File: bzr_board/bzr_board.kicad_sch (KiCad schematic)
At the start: 13 parts, among them J1 Conn_01x06, U1 74HC00

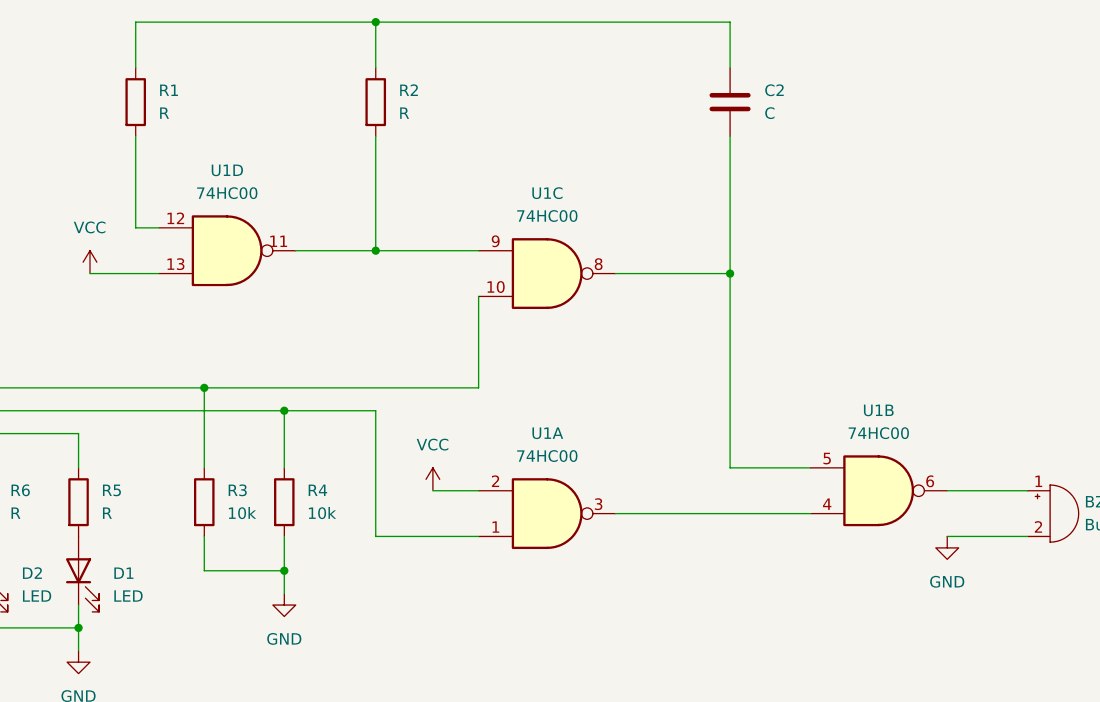
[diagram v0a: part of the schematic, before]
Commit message: bzr_board: update schematics and assign footprints
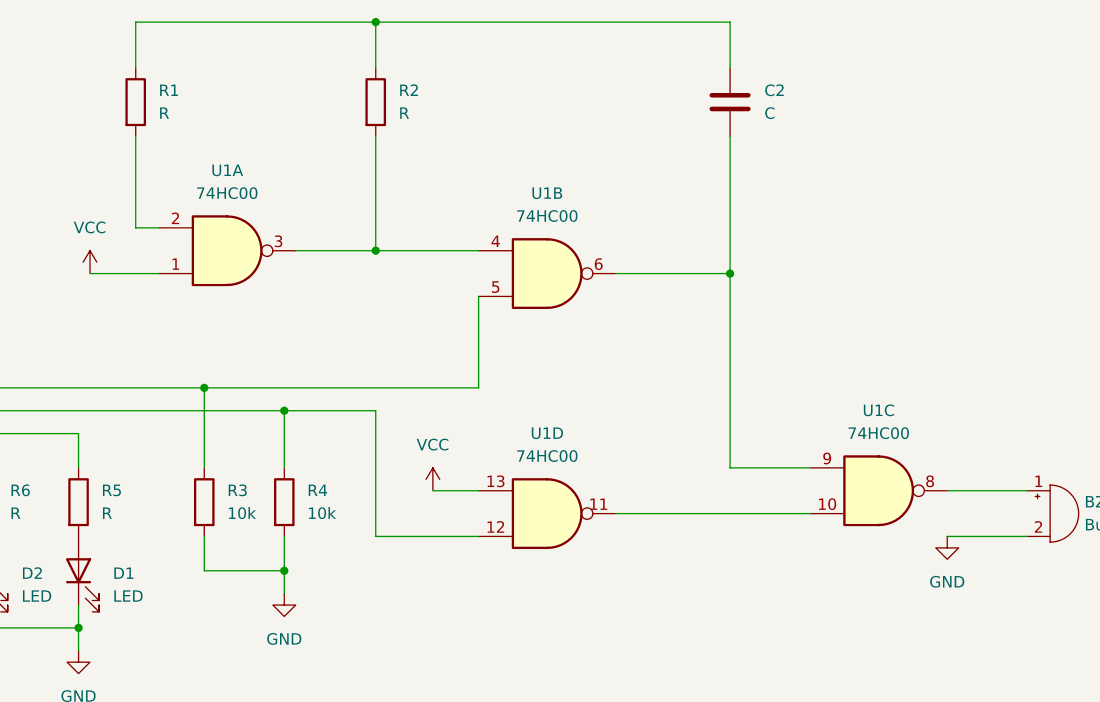
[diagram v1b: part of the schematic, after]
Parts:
- BZ1: footprint (none) -> Buzzer_Beeper:Buzzer_TDK_PS1240P02BT_D12.2mm_H6.5mm
- C1, C2: footprint (none) -> Capacitor_SMD:C_0805_2012Metric_Pad1.18x1.45mm_HandSolder
- D1, D2: footprint (none) -> LED_SMD:LED_0805_2012Metric_Pad1.15x1.40mm_HandSolder
- J1: footprint (none) -> Connector_PinHeader_2.54mm:PinHeader_1x06_P2.54mm_Vertical
- R1: footprint (none) -> Resistor_SMD:R_0603_1608Metric_Pad0.98x0.95mm_HandSolder
- R2, R3, R4, R5, R6: footprint (none) -> Resistor_SMD:R_0805_2012Metric_Pad1.20x1.40mm_HandSolder
- U1: footprint (none) -> Package_SO:SO-14_5.3x10.2mm_P1.27mm
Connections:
- net VCC: now also U1.1; no longer U1.2
- net auto: now also U1.5; no longer U1.10
- net manual: now also U1.12; no longer U1.1
- net at BZ1.1 (-): now also U1.8; no longer U1.6
- net at R1.2: now also U1.2; no longer U1.12
- net at U1.3, U1.4: now also R2.2
- new net: U1.10, U1.11
- new net: C2.2, U1.6, U1.9
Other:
- moved on the sheet: U1A, U1B, U1C, U1D

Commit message: bzr_board: add board design
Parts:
- R1: footprint Resistor_SMD:R_0603_1608Metric_Pad0.98x0.95mm_HandSolder -> Resistor_SMD:R_0805_2012Metric_Pad1.20x1.40mm_HandSolder
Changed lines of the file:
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@@
       (effects (font (size 1.27 1.27)) (justify left))
     )
-    (property "Footprint" "Resistor_SMD:R_0603_1608Metric_Pad0.98x0.95mm_HandSolder" (id 2) (at 109.982 38.1 90)
+    (property "Footprint" "Resistor_SMD:R_0805_2012Metric_Pad1.20x1.40mm_HandSolder" (id 2) (at 109.982 38.1 90)
       (effects (font (size 1.27 1.27)) hide)
     )
@@
     )
     (path "/fe3afa16-4331-4114-bcf8-f31acd774c30"
-      (reference "R1") (unit 1) (value "R") (footprint "Resistor_SMD:R_0603_1608Metric_Pad0.98x0.95mm_HandSolder")
+      (reference "R1") (unit 1) (value "R") (footprint "Resistor_SMD:R_0805_2012Metric_Pad1.20x1.40mm_HandSolder")
     )
     (path "/cccd4cea-c88e-4fc0-907f-447edef8bc42"

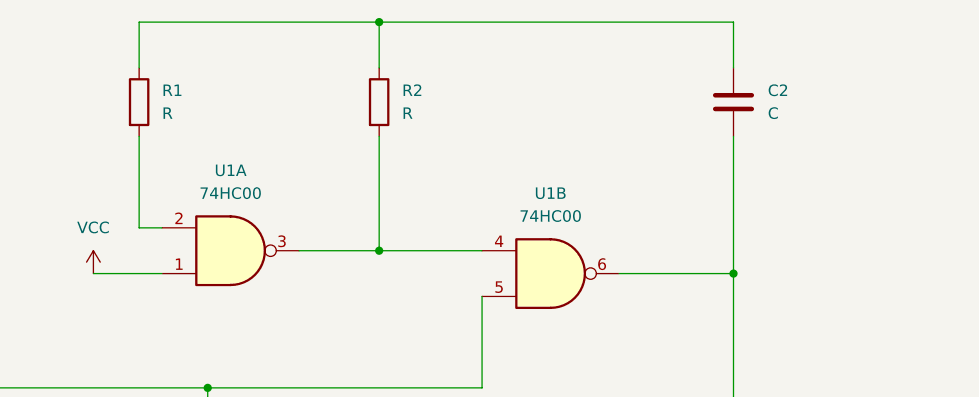
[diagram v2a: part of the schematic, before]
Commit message: bzr_board: set values for generating sound signal
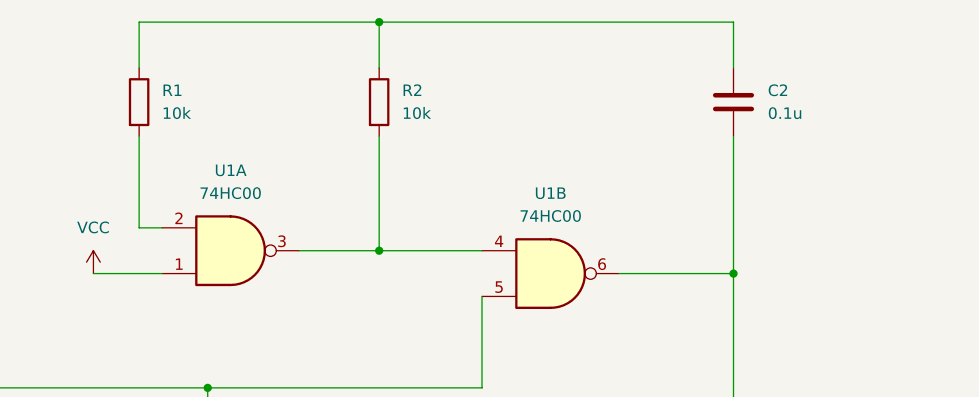
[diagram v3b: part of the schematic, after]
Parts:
- C2: value C -> 0.1u
- R1, R2: value R -> 10k
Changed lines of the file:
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@@
       (effects (font (size 1.27 1.27)) (justify left))
     )
-    (property "Value" "R" (id 1) (at 140.97 39.3699 0)
+    (property "Value" "10k" (id 1) (at 140.97 39.3699 0)
       (effects (font (size 1.27 1.27)) (justify left))
     )
@@
       (effects (font (size 1.27 1.27)) (justify left))
     )
-    (property "Value" "C" (id 1) (at 181.61 39.3699 0)
+    (property "Value" "0.1u" (id 1) (at 181.61 39.3699 0)
       (effects (font (size 1.27 1.27)) (justify left))
     )
@@
       (effects (font (size 1.27 1.27)) (justify left))
     )
-    (property "Value" "R" (id 1) (at 114.3 39.3699 0)
+    (property "Value" "10k" (id 1) (at 114.3 39.3699 0)
       (effects (font (size 1.27 1.27)) (justify left))
     )
@@
     )
     (path "/efeec5a0-dbab-4cee-92dc-a764fe254bfb"
-      (reference "C2") (unit 1) (value "C") (footprint "Capacitor_SMD:C_0805_2012Metric_Pad1.18x1.45mm_HandSolder")
+      (reference "C2") (unit 1) (value "0.1u") (footprint "Capacitor_SMD:C_0805_2012Metric_Pad1.18x1.45mm_HandSolder")
     )
     (path "/5c6f857d-da36-4799-8b62-cfec1ac8a07c"
@@
     )
     (path "/fe3afa16-4331-4114-bcf8-f31acd774c30"
-      (reference "R1") (unit 1) (value "R") (footprint "Resistor_SMD:R_0805_2012Metric_Pad1.20x1.40mm_HandSolder")
+      (reference "R1") (unit 1) (value "10k") (footprint "Resistor_SMD:R_0805_2012Metric_Pad1.20x1.40mm_HandSolder")
     )
     (path "/cccd4cea-c88e-4fc0-907f-447edef8bc42"
-      (reference "R2") (unit 1) (value "R") (footprint "Resistor_SMD:R_0805_2012Metric_Pad1.20x1.40mm_HandSolder")
+      (reference "R2") (unit 1) (value "10k") (footprint "Resistor_SMD:R_0805_2012Metric_Pad1.20x1.40mm_HandSolder")
     )
     (path "/2f965ec6-eebf-4f70-bea4-b474e7279464"
